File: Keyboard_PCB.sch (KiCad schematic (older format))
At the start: 9 parts, among them CON1 PS/2_JACK, U1 ATMEGA32M1, X1 CRYSTAL

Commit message: Changed things.
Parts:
- removed U1: ATMEGA32M1, symbol ATMEGA32M1
- added R2: RESISTOR, symbol RESISTOR
- added S1: SPEAKER, ~, symbol SPEAKER
- added U?: ATMEGA328, symbol ATMEGA328
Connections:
- wire segments 44 -> 54
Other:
- moved on the sheet: C1, C2, CON1, R1, X1

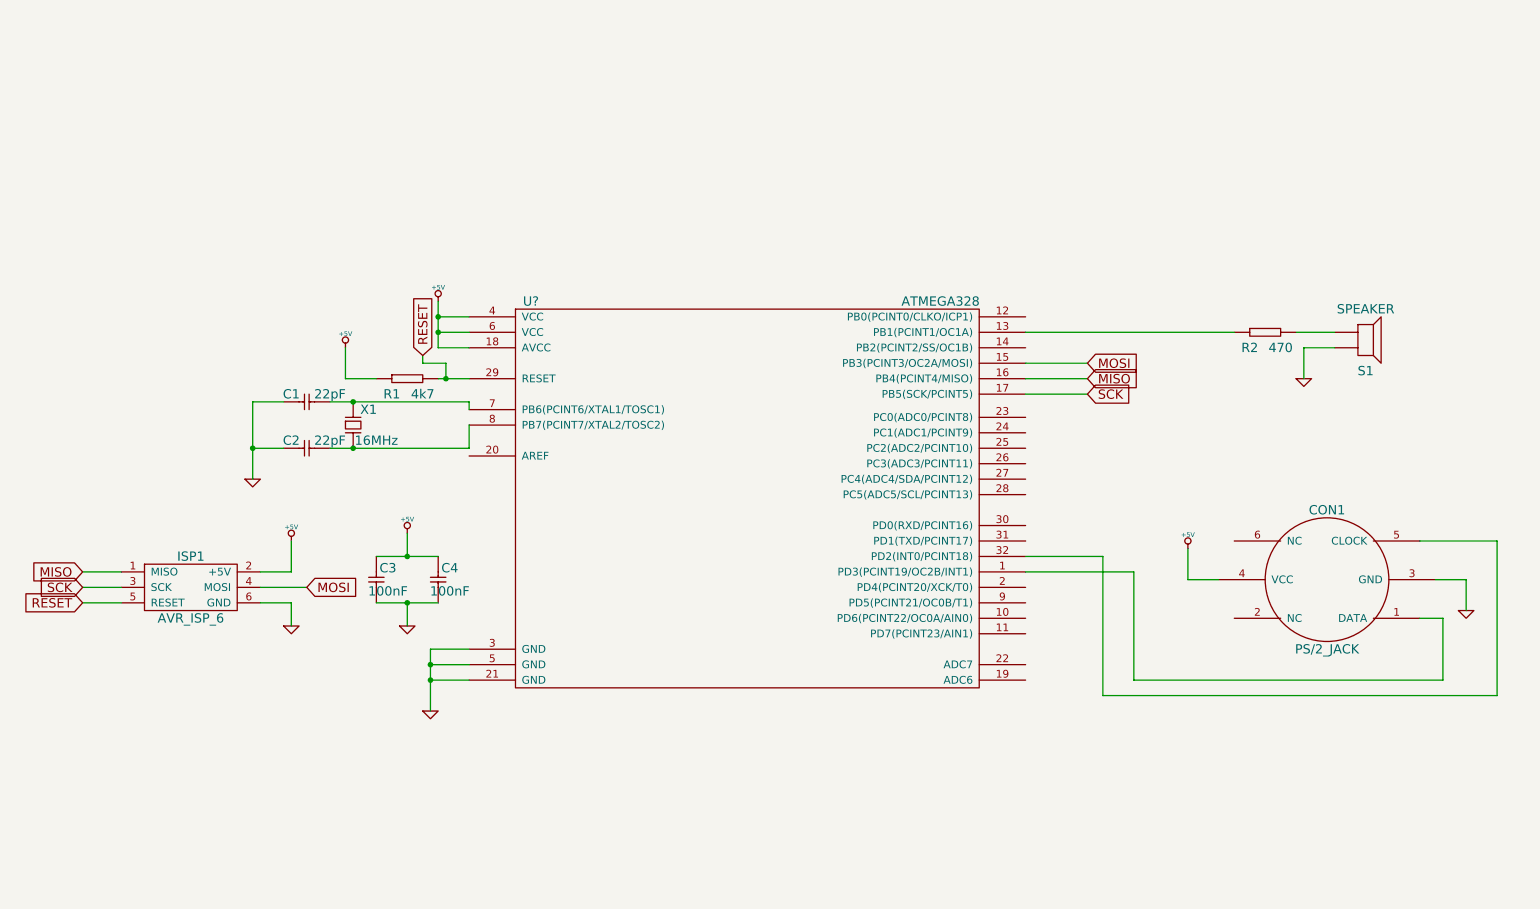
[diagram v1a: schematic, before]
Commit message: Added FTDI and USB
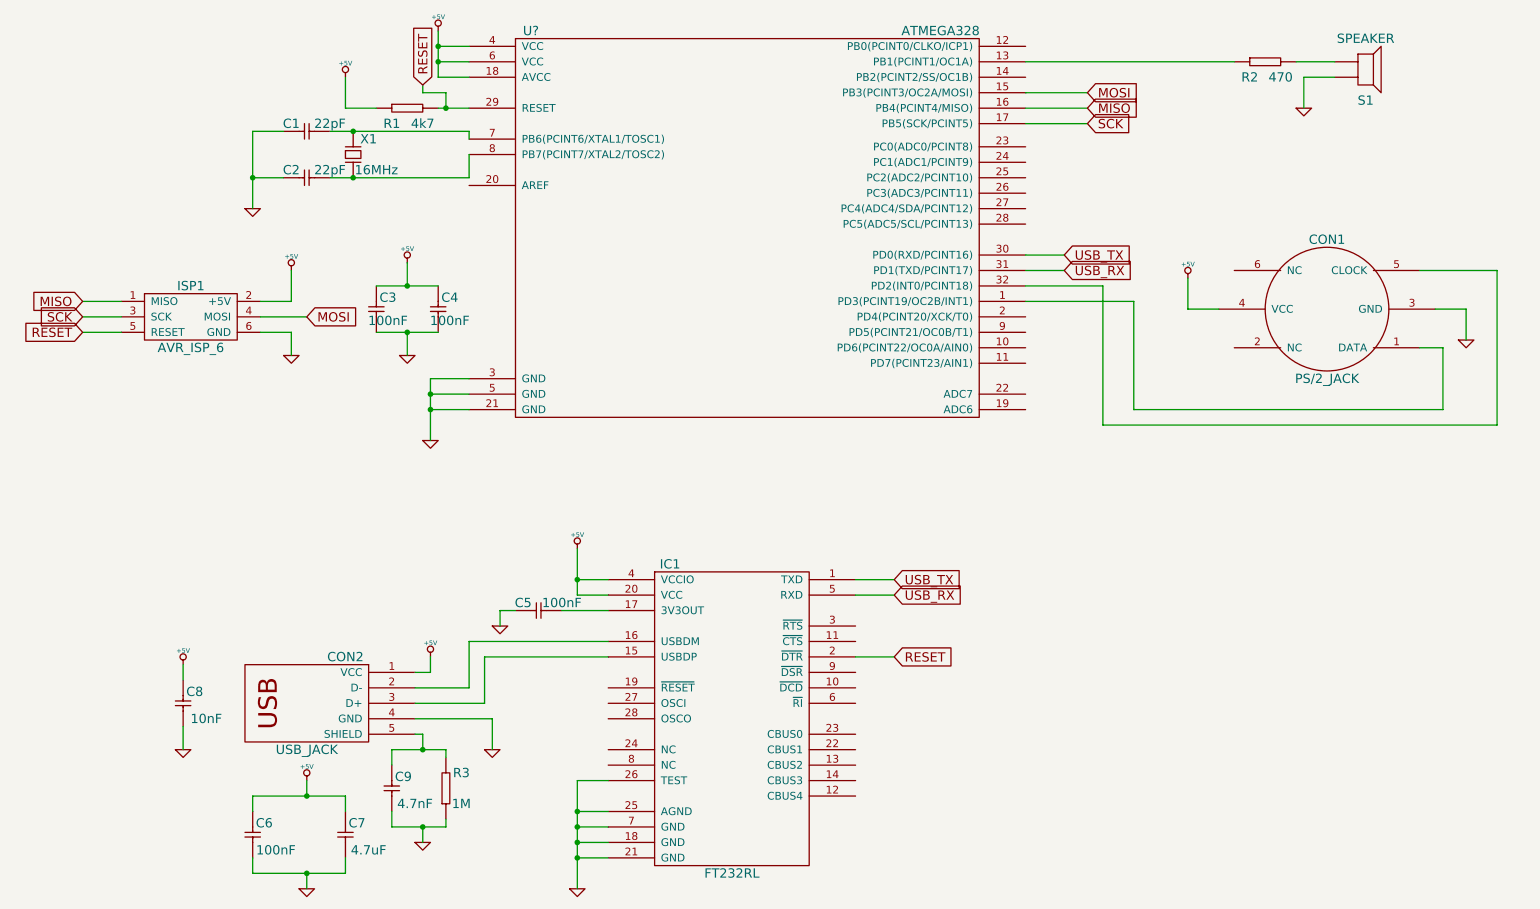
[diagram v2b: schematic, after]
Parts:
- added C5, C6, C7, C8, C9: CAPACITOR, symbol CAPACITOR
- added CON2: USB_JACK, symbol USB_JACK
- added IC1: FT232RL, symbol FT232RL
- added R3: RESISTOR, symbol RESISTOR
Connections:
- net +5V: now also C6.1, C7.1, C8.1, CON2.1 (VCC), IC1.20 (VCC), IC1.4 (VCCIO)
- net GND: now also C5.1, C6.2, C7.2, C8.2, C9.2, CON2.4 (GND), IC1.18 (GND), IC1.21 (GND), IC1.25 (AGND), IC1.26 (TEST), IC1.7 (GND), R3.1
- net RESET: now also IC1.2 (~DTR)
- net USB_TX: now reaches U?.30 (PD0(RXD/PCINT16))
- net USB_TX: now also IC1.1 (TXD)
- net USB_RX: now reaches U?.31 (PD1(TXD/PCINT17))
- net USB_RX: now also IC1.5 (RXD)
- new net: CON2.3 (D+), IC1.15 (USBDP)
- new net: CON2.2 (D-), IC1.16 (USBDM)
- new net: C5.2, IC1.17 (3V3OUT)
- new net: C9.1, CON2.5 (SHIELD), R3.2
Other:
- moved on the sheet: C1, C2, C3, C4, CON1, ISP1, R1, R2, S1, U?, X1

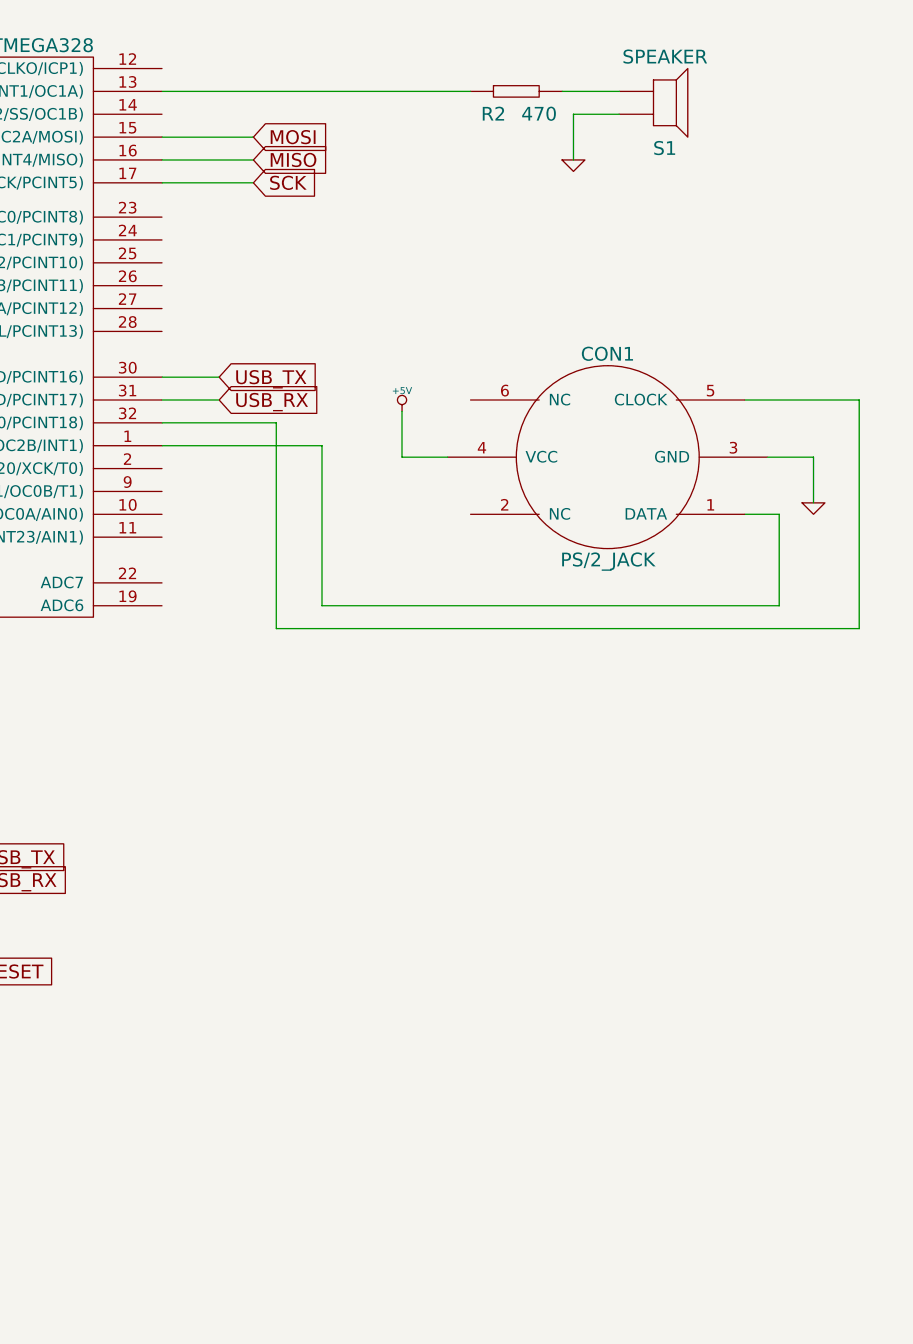
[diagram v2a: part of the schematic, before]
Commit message: Added LCD Circuit.
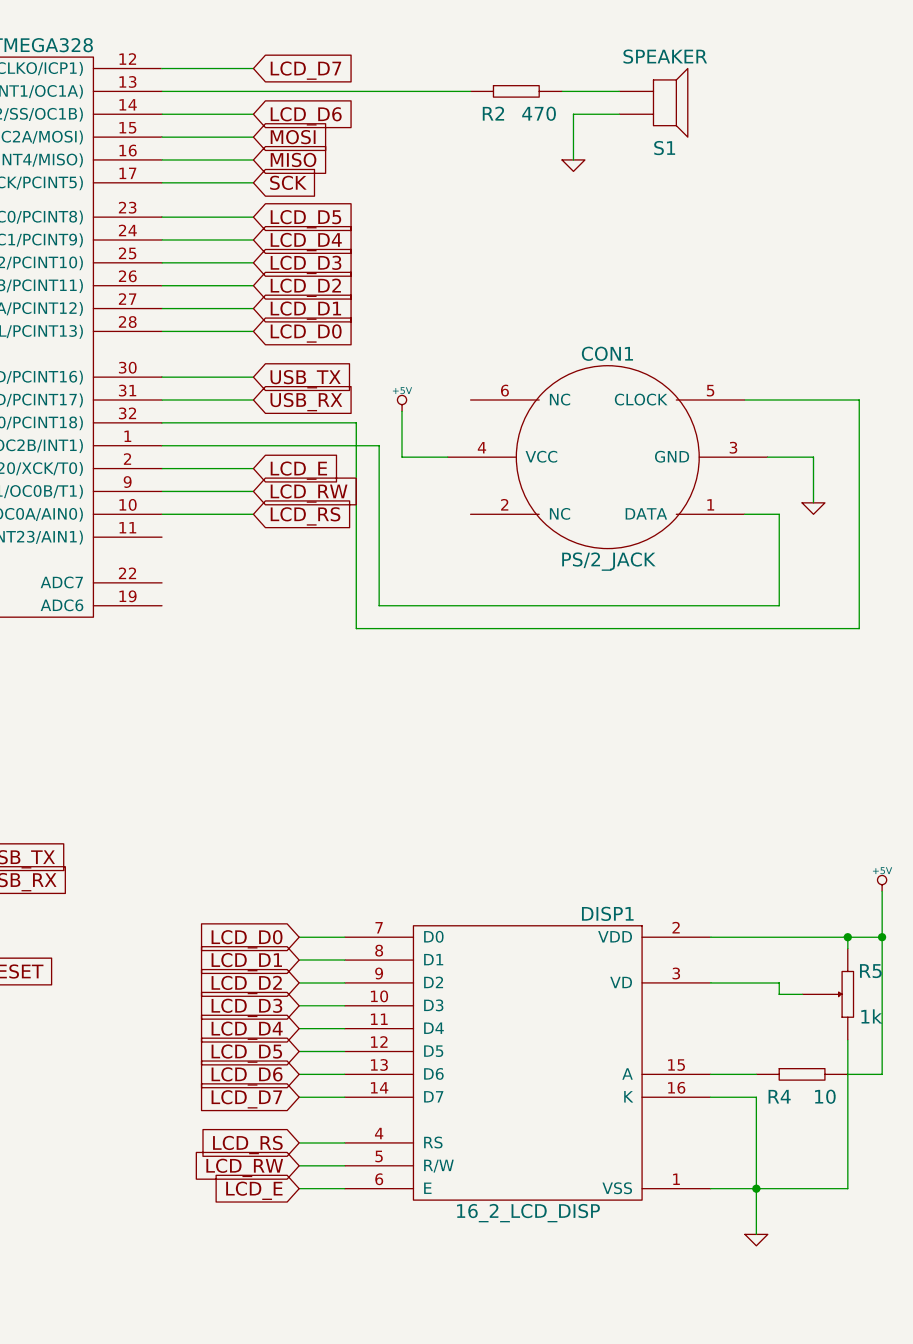
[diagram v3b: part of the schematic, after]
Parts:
- added DISP1: 16_2_LCD_DISP, symbol 16_2_LCD_DISP
- added R4: RESISTOR, symbol RESISTOR
- added R5: RESISTOR_VAR, symbol RESISTOR_VAR
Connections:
- net +5V: now also DISP1.2 (VDD), R4.2, R5.3
- net GND: now also DISP1.1 (VSS), DISP1.16 (K), R5.1
- net LCD_RS: now reaches U?.10 (PD6(PCINT22/OC0A/AIN0))
- net LCD_RS: now also DISP1.4 (RS)
- net LCD_D7: now reaches U?.12 (PB0(PCINT0/CLKO/ICP1))
- net LCD_D7: now also DISP1.14 (D7)
- net LCD_D6: now reaches U?.14 (PB2(PCINT2/SS/OC1B))
- net LCD_D6: now also DISP1.13 (D6)
- net LCD_E: now reaches U?.2 (PD4(PCINT20/XCK/T0))
- net LCD_E: now also DISP1.6 (E)
- net LCD_D5: now reaches U?.23 (PC0(ADC0/PCINT8))
- net LCD_D5: now also DISP1.12 (D5)
- net LCD_D4: now reaches U?.24 (PC1(ADC1/PCINT9))
- net LCD_D4: now also DISP1.11 (D4)
- net LCD_D3: now reaches U?.25 (PC2(ADC2/PCINT10))
- net LCD_D3: now also DISP1.10 (D3)
- net LCD_D2: now reaches U?.26 (PC3(ADC3/PCINT11))
- net LCD_D2: now also DISP1.9 (D2)
- net LCD_D1: now reaches U?.27 (PC4(ADC4/SDA/PCINT12))
- net LCD_D1: now also DISP1.8 (D1)
- net LCD_D0: now reaches U?.28 (PC5(ADC5/SCL/PCINT13))
- net LCD_D0: now also DISP1.7 (D0)
- net LCD_RW: now reaches U?.9 (PD5(PCINT21/OC0B/T1))
- net LCD_RW: now also DISP1.5 (R/W)
- new net: DISP1.15 (A), R4.1
- new net: DISP1.3 (VD), R5.2

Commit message: changed stuff.
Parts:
- added R6: RESISTOR_VAR, ~, symbol RESISTOR_VAR
- gave numbers to parts that had none: 1
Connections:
- net +5V: now also R6.3
- net GND: now also R6.1
- net at U1.19 (ADC6): now also R6.2
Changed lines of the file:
@@
 $EndDescr
 $Comp
-L GND #PWR?
+L GND #PWR01
 U 1 1 524AF34C
 P 10400 3000
-F 0 "#PWR?" H 10400 3000 30  0001 C CNN
+F 0 "#PWR01" H 10400 3000 30  0001 C CNN
 F 1 "GND" H 10400 2930 30  0001 C CNN
 F 2 "" H 10400 3000 60  0000 C CNN
@@
 $EndComp
 $Comp
-L +5V #PWR?
+L +5V #PWR02
 U 1 1 524AF39E
 P 8600 2600
-F 0 "#PWR?" H 8600 2690 20  0001 C CNN
+F 0 "#PWR02" H 8600 2690 20  0001 C CNN
 F 1 "+5V" H 8600 2690 30  0000 C CNN
 F 2 "" H 8600 2600 60  0000 C CNN
@@
 $EndComp
 $Comp
-L GND #PWR?
+L GND #PWR03
 U 1 1 524AF416
 P 3700 3650
-F 0 "#PWR?" H 3700 3650 30  0001 C CNN
+F 0 "#PWR03" H 3700 3650 30  0001 C CNN
 F 1 "GND" H 3700 3580 30  0001 C CNN
 F 2 "" H 3700 3650 60  0000 C CNN
@@
 $EndComp
 $Comp
-L +5V #PWR?
+L +5V #PWR04
 U 1 1 524AF453
 P 3750 1000
-F 0 "#PWR?" H 3750 1090 20  0001 C CNN
+F 0 "#PWR04" H 3750 1090 20  0001 C CNN
 F 1 "+5V" H 3750 1090 30  0000 C CNN
 F 2 "" H 3750 1000 60  0000 C CNN
@@
 $EndComp
 $Comp
-L +5V #PWR?
+L +5V #PWR05
 U 1 1 524AF516
 P 3150 1300
-F 0 "#PWR?" H 3150 1390 20  0001 C CNN
+F 0 "#PWR05" H 3150 1390 20  0001 C CNN
 F 1 "+5V" H 3150 1390 30  0000 C CNN
 F 2 "" H 3150 1300 60  0000 C CNN
@@
 $EndComp
 $Comp
-L GND #PWR?
+L GND #PWR06
 U 1 1 524AF67E
 P 2550 2150
-F 0 "#PWR?" H 2550 2150 30  0001 C CNN
+F 0 "#PWR06" H 2550 2150 30  0001 C CNN
 F 1 "GND" H 2550 2080 30  0001 C CNN
 F 2 "" H 2550 2150 60  0000 C CNN
@@
 $EndComp
 $Comp
-L GND #PWR?
+L GND #PWR07
 U 1 1 524AF808
 P 3550 3100
-F 0 "#PWR?" H 3550 3100 30  0001 C CNN
+F 0 "#PWR07" H 3550 3100 30  0001 C CNN
 F 1 "GND" H 3550 3030 30  0001 C CNN
 F 2 "" H 3550 3100 60  0000 C CNN
@@
 $EndComp
 $Comp
-L +5V #PWR?
+L +5V #PWR08
 U 1 1 524AF87D
 P 3550 2500
-F 0 "#PWR?" H 3550 2590 20  0001 C CNN
+F 0 "#PWR08" H 3550 2590 20  0001 C CNN
 F 1 "+5V" H 3550 2590 30  0000 C CNN
 F 2 "" H 3550 2500 60  0000 C CNN
@@
 SCK
 $Comp
-L GND #PWR?
+L GND #PWR09
 U 1 1 524AFAB9
 P 2800 3100
-F 0 "#PWR?" H 2800 3100 30  0001 C CNN
+F 0 "#PWR09" H 2800 3100 30  0001 C CNN
 F 1 "GND" H 2800 3030 30  0001 C CNN
 F 2 "" H 2800 3100 60  0000 C CNN
@@
 $EndComp
 $Comp
-L +5V #PWR?
+L +5V #PWR010
 U 1 1 524AFAED
 P 2800 2550
-F 0 "#PWR?" H 2800 2640 20  0001 C CNN
+F 0 "#PWR010" H 2800 2640 20  0001 C CNN
 F 1 "+5V" H 2800 2640 30  0000 C CNN
 F 2 "" H 2800 2550 60  0000 C CNN
@@
 $EndComp
 $Comp
-L GND #PWR?
+L GND #PWR011
 U 1 1 524D5161
 P 9350 1500
-F 0 "#PWR?" H 9350 1500 30  0001 C CNN
+F 0 "#PWR011" H 9350 1500 30  0001 C CNN
 F 1 "GND" H 9350 1430 30  0001 C CNN
 F 2 "" H 9350 1500 60  0000 C CNN
@@
 $EndComp
 $Comp
-L ATMEGA328 U?
+L ATMEGA328 U1
 U 1 1 524D729E
 P 5750 2300
-F 0 "U?" H 4350 3600 60  0000 C CNN
+F 0 "U1" H 4350 3600 60  0000 C CNN
 F 1 "ATMEGA328" H 7000 3600 60  0000 C CNN
 F 2 "" H 7450 3000 60  0000 C CNN
@@
 $EndComp
 $Comp
-L +5V #PWR?
+L +5V #PWR012
 U 1 1 524FF695
 P 4650 4350
-F 0 "#PWR?" H 4650 4440 20  0001 C CNN
+F 0 "#PWR012" H 4650 4440 20  0001 C CNN
 F 1 "+5V" H 4650 4440 30  0000 C CNN
 F 2 "" H 4650 4350 60  0000 C CNN
@@
 $EndComp
 $Comp
-L GND #PWR?
+L GND #PWR013
 U 1 1 524FF80E
 P 4150 4850
-F 0 "#PWR?" H 4150 4850 30  0001 C CNN
+F 0 "#PWR013" H 4150 4850 30  0001 C CNN
 F 1 "GND" H 4150 4780 30  0001 C CNN
 F 2 "" H 4150 4850 60  0000 C CNN
@@
 $EndComp
 $Comp
-L GND #PWR?
+L GND #PWR014
 U 1 1 524FF8B3
 P 4650 6550
-F 0 "#PWR?" H 4650 6550 30  0001 C CNN
+F 0 "#PWR014" H 4650 6550 30  0001 C CNN
 F 1 "GND" H 4650 6480 30  0001 C CNN
 F 2 "" H 4650 6550 60  0000 C CNN
@@
 $EndComp
 $Comp
-L +5V #PWR?
+L +5V #PWR015
 U 1 1 524FFD30
 P 2900 5850
-F 0 "#PWR?" H 2900 5940 20  0001 C CNN
+F 0 "#PWR015" H 2900 5940 20  0001 C CNN
 F 1 "+5V" H 2900 5940 30  0000 C CNN
 F 2 "" H 2900 5850 60  0000 C CNN
@@
 $EndComp
 $Comp
-L GND #PWR?
+L GND #PWR016
 U 1 1 524FFD3F
 P 2900 6550
-F 0 "#PWR?" H 2900 6550 30  0001 C CNN
+F 0 "#PWR016" H 2900 6550 30  0001 C CNN
 F 1 "GND" H 2900 6480 30  0001 C CNN
 F 2 "" H 2900 6550 60  0000 C CNN
@@
 $EndComp
 $Comp
-L +5V #PWR?
+L +5V #PWR017
 U 1 1 525000B4
 P 3700 5050
-F 0 "#PWR?" H 3700 5140 20  0001 C CNN
+F 0 "#PWR017" H 3700 5140 20  0001 C CNN
 F 1 "+5V" H 3700 5140 30  0000 C CNN
 F 2 "" H 3700 5050 60  0000 C CNN
@@
 $EndComp
 $Comp
-L GND #PWR?
+L GND #PWR018
 U 1 1 525001F0
 P 4100 5650
-F 0 "#PWR?" H 4100 5650 30  0001 C CNN
+F 0 "#PWR018" H 4100 5650 30  0001 C CNN
 F 1 "GND" H 4100 5580 30  0001 C CNN
 F 2 "" H 4100 5650 60  0000 C CNN
@@
 $EndComp
 $Comp
-L GND #PWR?
+L GND #PWR019
 U 1 1 525002B7
 P 2100 5650
-F 0 "#PWR?" H 2100 5650 30  0001 C CNN
+F 0 "#PWR019" H 2100 5650 30  0001 C CNN
 F 1 "GND" H 2100 5580 30  0001 C CNN
 F 2 "" H 2100 5650 60  0000 C CNN
@@
 $EndComp
 $Comp
-L +5V #PWR?
+L +5V #PWR020
 U 1 1 525002C6
 P 2100 5100
-F 0 "#PWR?" H 2100 5190 20  0001 C CNN
+F 0 "#PWR020" H 2100 5190 20  0001 C CNN
 F 1 "+5V" H 2100 5190 30  0000 C CNN
 F 2 "" H 2100 5100 60  0000 C CNN
@@
 $EndComp
 $Comp
-L GND #PWR?
+L GND #PWR021
 U 1 1 52500609
 P 3650 6250
-F 0 "#PWR?" H 3650 6250 30  0001 C CNN
+F 0 "#PWR021" H 3650 6250 30  0001 C CNN
 F 1 "GND" H 3650 6180 30  0001 C CNN
 F 2 "" H 3650 6250 60  0000 C CNN
@@
 $EndComp
 $Comp
-L GND #PWR?
+L GND #PWR022
 U 1 1 52500CE1
 P 10150 6200
-F 0 "#PWR?" H 10150 6200 30  0001 C CNN
+F 0 "#PWR022" H 10150 6200 30  0001 C CNN
 F 1 "GND" H 10150 6130 30  0001 C CNN
 F 2 "" H 10150 6200 60  0000 C CNN
@@
 $EndComp
 $Comp
-L +5V #PWR?
+L +5V #PWR023
 U 1 1 52500E1D
 P 10700 4700
-F 0 "#PWR?" H 10700 4790 20  0001 C CNN
+F 0 "#PWR023" H 10700 4790 20  0001 C CNN
 F 1 "+5V" H 10700 4790 30  0000 C CNN
 F 2 "" H 10700 4700 60  0000 C CNN
@@
 Wire Wire Line
 	10550 6000 10550 5350
+$Comp
+L RESISTOR_VAR R6
+U 1 1 525037D7
+P 7950 3650
+F 0 "R6" H 8050 3750 60  0000 C CNN
+F 1 "RESISTOR_VAR" V 7950 3650 60  0001 C CNN
+F 2 "~" H 7950 3450 60  0000 C CNN
+F 3 "~" H 7950 3450 60  0000 C CNN
+F 4 "10k" H 8150 3550 60  0000 C CNN "Resistance"
+	1    7950 3650
+	1    0    0    -1
+$EndComp
+$Comp
+L +5V #PWR024
+U 1 1 5250380F
+P 7950 3350
+F 0 "#PWR024" H 7950 3440 20  0001 C CNN
+F 1 "+5V" H 7950 3440 30  0000 C CNN
+F 2 "" H 7950 3350 60  0000 C CNN
+F 3 "" H 7950 3350 60  0000 C CNN
+	1    7950 3350
+	1    0    0    -1
+$EndComp
+$Comp
+L GND #PWR025
+U 1 1 5250382A
+P 7950 4000
+F 0 "#PWR025" H 7950 4000 30  0001 C CNN
+F 1 "GND" H 7950 3930 30  0001 C CNN
+F 2 "" H 7950 4000 60  0000 C CNN
+F 3 "" H 7950 4000 60  0000 C CNN
+	1    7950 4000
+	1    0    0    -1
+$EndComp
+Wire Wire Line
+	7950 4000 7950 3850
+Wire Wire Line
+	7950 3450 7950 3350
+Wire Wire Line
+	7750 3650 7550 3650
+Wire Wire Line
+	7550 3650 7550 3450
 $EndSCHEMATC

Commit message: Didn't change much, just a bit.
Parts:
- R6: footprint ~ -> (none)
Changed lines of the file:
@@
 LIBS:Power_Sym
 LIBS:Keyboard_PCB-cache
-EELAYER 27 0
+EELAYER 24 0
 EELAYER END
 $Descr A4 11693 8268
@@
 Wire Wire Line
 	7550 3050 7950 3050
-$Comp
-L RESISTOR_VAR R5
-U 1 1 525027C8
-P 10550 5150
-F 0 "R5" H 10650 5250 60  0000 C CNN
-F 1 "RESISTOR_VAR" V 10550 5150 60  0001 C CNN
-F 2 "" H 10550 4950 60  0000 C CNN
-F 3 "" H 10550 4950 60  0000 C CNN
-F 4 "1k" H 10650 5050 60  0000 C CNN "Resistance"
-	1    10550 5150
-	1    0    0    -1
-$EndComp
 Wire Wire Line
 	9950 5100 10250 5100
@@
 Wire Wire Line
 	10550 6000 10550 5350
-$Comp
-L RESISTOR_VAR R6
-U 1 1 525037D7
-P 7950 3650
-F 0 "R6" H 8050 3750 60  0000 C CNN
-F 1 "RESISTOR_VAR" V 7950 3650 60  0001 C CNN
-F 2 "~" H 7950 3450 60  0000 C CNN
-F 3 "~" H 7950 3450 60  0000 C CNN
-F 4 "10k" H 8150 3550 60  0000 C CNN "Resistance"
-	1    7950 3650
-	1    0    0    -1
-$EndComp
 $Comp
 L +5V #PWR024
@@
 Wire Wire Line
 	7550 3650 7550 3450
+$Comp
+L RESISTOR_VAR R6
+U 1 1 525311F0
+P 7950 3650
+F 0 "R6" H 8050 3750 60  0000 C CNN
+F 1 "RESISTOR_VAR" V 7950 3650 60  0001 C CNN
+F 2 "" H 7950 3450 60  0000 C CNN
+F 3 "" H 7950 3450 60  0000 C CNN
+F 4 "10k" H 8100 3550 60  0000 C CNN "Resistance"
+	1    7950 3650
+	1    0    0    -1
+$EndComp
+$Comp
+L RESISTOR_VAR R5
+U 1 1 52531227
+P 10550 5150
+F 0 "R5" H 10650 5250 60  0000 C CNN
+F 1 "RESISTOR_VAR" V 10550 5150 60  0001 C CNN
+F 2 "" H 10550 4950 60  0000 C CNN
+F 3 "" H 10550 4950 60  0000 C CNN
+F 4 "1k" H 10650 5050 60  0000 C CNN "Resistance"
+	1    10550 5150
+	1    0    0    -1
+$EndComp
 $EndSCHEMATC
